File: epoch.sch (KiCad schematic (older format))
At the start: 32 parts, among them P1 USB_OTG, P2 BATT, P3 CONN_01X10, P4 CONN_02X05, Q1 Q_PMOS_DGS, SW1 SW_Push, U1 MIC5219-3.3BM5, U2 ATSAMD21Ennc-AU, U3 MCP73831T-2ACI/OT, U4 MCP7940N-I/SN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

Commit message: Link buttons and add PCB
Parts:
- removed 10K1: R, symbol R
- removed C10: 1uF, symbol C_Small
- removed D1: LED, symbol LED
- removed D2: ZLLS410, symbol D
- removed P2: BATT, symbol CONN_01X02
- removed Q1: Q_PMOS_DGS, symbol Q_PMOS_DGS
- removed R4: 47K, symbol R
- removed U3: MCP73831T-2ACI/OT, smd-semi:SOT-23-5, symbol MCP73831T-2ACI/OT
- removed U4: MCP7940N-I/SN, IPC7351-Nominal:SOIC127P600X175-8, symbol MCP7940N-I/SN
- removed Y2: 32.768kHz, symbol Crystal
- added SW2: SW_Up, Buttons_Switches_THT:SW_PUSH_SMALL, symbol SW_Push
- added SW3: SW_Middle, Buttons_Switches_THT:SW_PUSH_SMALL, symbol SW_Push
- added SW4: SW_Down, Buttons_Switches_THT:SW_PUSH_SMALL, symbol SW_Push
- added U3: DS3231MZ, Housings_SOIC:SOIC-8_3.9x4.9mm_Pitch1.27mm, symbol DS3231MZ
- C1, C11, C2, C3, C5, C6: footprint (none) -> Capacitors_SMD:C_0805_HandSoldering
- C4, C9: value 4.7uF -> 0.1uF; footprint (none) -> Capacitors_SMD:C_0805_HandSoldering
- C7, C8: value 22uF -> ??uF; footprint (none) -> Capacitors_SMD:C_0805_HandSoldering
- P1: footprint (none) -> Connectors_Molex:USB_Micro-B_Molex_47346-0001
- P3: footprint (none) -> Connector_FFC_FPC:MOLEX_0.5MM_505278
- P4: footprint (none) -> Pin_Headers:Pin_Header_Straight_2x05_Pitch1.27mm_SMD
- R1: value 220 -> 249; footprint (none) -> Resistors_SMD:R_0805_HandSoldering
- R2: value 5K6 -> 4.7K; footprint (none) -> Resistors_SMD:R_0805_HandSoldering
- R3: value 47K -> 4.7K; footprint (none) -> Resistors_SMD:R_0805_HandSoldering
- R5: footprint (none) -> Resistors_SMD:R_0805_HandSoldering
- SW1: value SW_Push -> SW_Reset; footprint (none) -> Buttons_Switches_THT:SW_PUSH_SMALL
- U2: footprint IPC7351-Nominal:QFP80P900X900X120-32 -> Housings_QFP:TQFP-32_7x7mm_Pitch0.8mm
- U5: footprint (none) -> TO_SOT_Packages_SMD:SOT-353_SC-70-5_Handsoldering
- Y1: footprint (none) -> Crystals:Crystals_Citizen_CM200C_7.9_x_3.7
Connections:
- net labels added: BUT_DWN, BUT_MID, BUT_UP
- net labels removed: (+5), PWR_SENSE, STAT, SWCLK
- wire segments 116 -> 93
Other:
- note added: "Real Time clock and VCOM refresh"
- note added: "USB"
- note removed: "USB Charging Circuit"
- moved on the sheet: C1, C2, C3, C5, C6, C7, C8, P1, R5, SW1, U1, U2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

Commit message: More Layout
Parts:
- removed P1: USB_OTG, Connectors_Molex:USB_Micro-B_Molex_47346-0001, symbol USB_OTG
- added J1: USB_OTG, Connectors:USB-MICROB_LARGEPAD, symbol USB_OTG
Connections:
- net (GND): now also J1.5 (GND), J1.6 (Shield)
- net USB_D+: now also J1.3 (D+)
- net USB_D-: now also J1.2 (D-)
- net at U1.1 (IN), U1.3 (EN): now also J1.1 (VBUS)
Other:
- note removed: "USB"
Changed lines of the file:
@@
 RESET
-$Comp
-L USB_OTG P1
-U 1 1 58B3A824
-P 1750 1350
-F 0 "P1" H 1900 950 50  0000 C CNN
-F 1 "USB_OTG" H 1750 1700 50  0000 C CNN
-F 2 "Connectors_Molex:USB_Micro-B_Molex_47346-0001" V 1700 1250 50  0001 C CNN
-F 3 "" V 1700 1250 50  0000 C CNN
-	1    1750 1350
-	1    0    0    1
-$EndComp
 $Comp
 L (GND) #PWR010
 U 1 1 58B3A991
-P 1450 1850
-F 0 "#PWR010" H 1450 1850 30  0001 C CNN
-F 1 "(GND)" H 1450 1850 30  0001 C CNN
-F 2 "" H 1450 1850 60  0000 C CNN
-F 3 "" H 1450 1850 60  0000 C CNN
-	1    1450 1850
+P 1600 2000
+F 0 "#PWR010" H 1600 2000 30  0001 C CNN
+F 1 "(GND)" H 1600 2000 30  0001 C CNN
+F 2 "" H 1600 2000 60  0000 C CNN
+F 3 "" H 1600 2000 60  0000 C CNN
+	1    1600 2000
 	-1   0    0    -1
 $EndComp
-Text GLabel 2050 1250 2    60   BiDi ~ 0
+Text GLabel 2000 1500 2    60   BiDi ~ 0
 USB_D-
-Text GLabel 2050 1350 2    60   BiDi ~ 0
+Text GLabel 2000 1400 2    60   BiDi ~ 0
 USB_D+
 $Comp
@@
 	1    0    0    -1
 $EndComp
-Wire Wire Line
-	2800 1250 3050 1250
 $Comp
 L (GND) #PWR011
@@
 Wire Wire Line
 	4350 1150 4350 1200
-Text Notes 1550 850  0    60   ~ 0
-USB
 Text Notes 3050 850  0    60   ~ 0
 3.3V Regulator
@@
 	8500 2150 8500 2600
 Wire Wire Line
-	1650 950  1650 900
-Wire Wire Line
-	1450 900  1750 900
-Wire Wire Line
-	1450 900  1450 1850
-Wire Wire Line
-	1750 900  1750 950
-Connection ~ 1650 900
-Wire Wire Line
-	2800 1550 2050 1550
-Wire Wire Line
-	2800 1150 2800 1550
+	2800 1150 2800 1250
 Wire Wire Line
 	2800 1150 3050 1150
-Connection ~ 2800 1250
+Connection ~ 2800 1200
 $Comp
 L SW_Push SW2
@@
 SDA
 Wire Wire Line
-	6600 1850 6400 1850
-Wire Wire Line
-	6600 1950 6000 1950
+	6400 1850 6600 1850
+Wire Wire Line
+	6000 1950 6600 1950
 $Comp
 L R R3
@@
 Connection ~ 6050 1950
 Wire Wire Line
-	6050 1500 6050 1350
+	6050 1350 6050 1500
 Wire Wire Line
 	6500 1850 6500 1800
@@
 Text GLabel 3750 4600 2    60   Input ~ 0
 BUT_UP
+$Comp
+L USB_OTG J1
+U 1 1 58F5A24A
+P 1700 1400
+F 0 "J1" H 1500 1850 50  0000 L CNN
+F 1 "USB_OTG" H 1500 1750 50  0000 L CNN
+F 2 "Connectors:USB-MICROB_LARGEPAD" H 1850 1350 50  0001 C CNN
+F 3 "" H 1850 1350 50  0001 C CNN
+	1    1700 1400
+	1    0    0    -1
+$EndComp
+Wire Wire Line
+	2800 1250 3050 1250
+Wire Wire Line
+	1600 1800 1600 2000
+Wire Wire Line
+	1700 1800 1700 1900
+Wire Wire Line
+	1700 1900 1600 1900
+Connection ~ 1600 1900
+Wire Wire Line
+	2000 1200 2800 1200
 $EndSCHEMATC

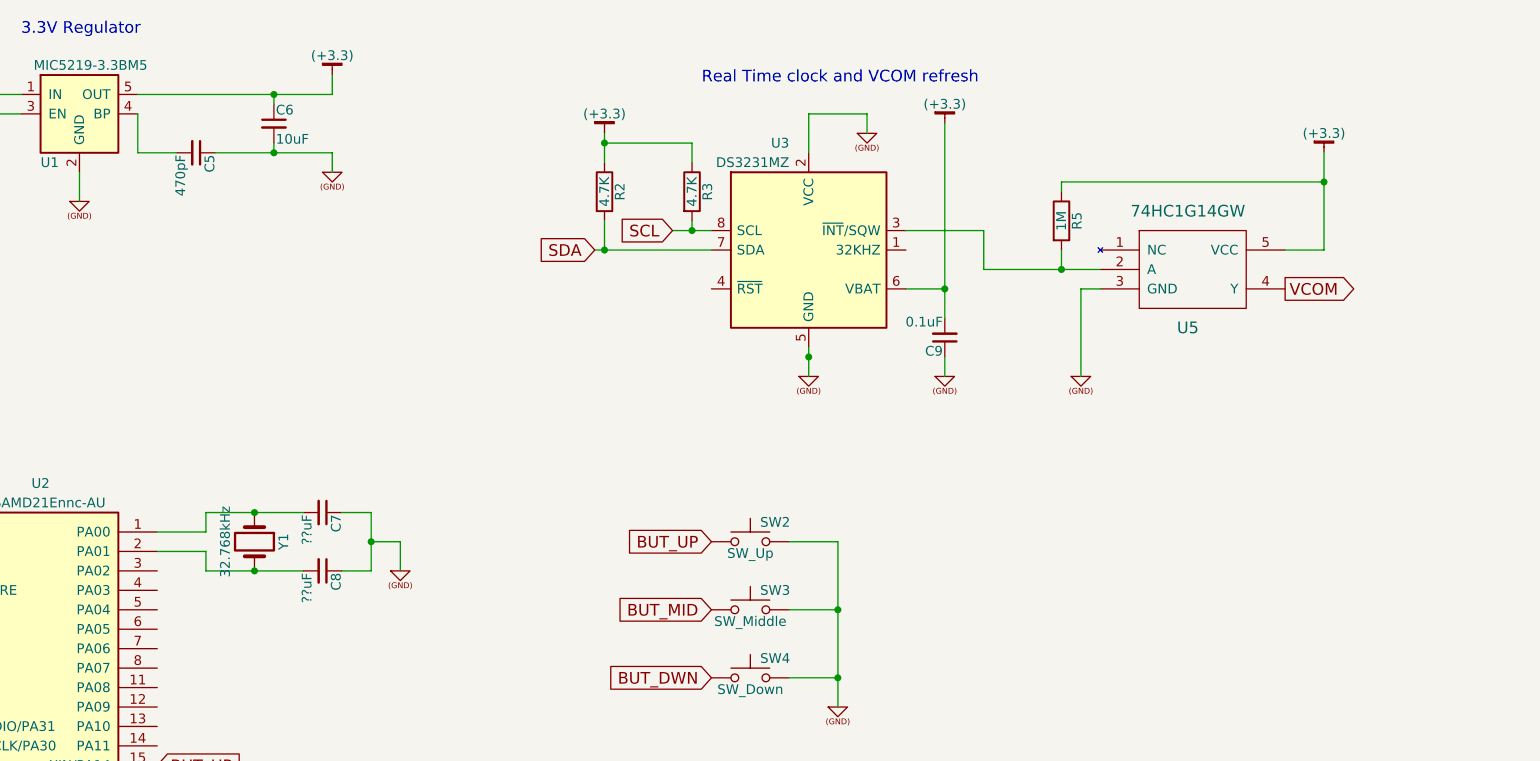
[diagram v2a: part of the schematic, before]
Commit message: Add coincell
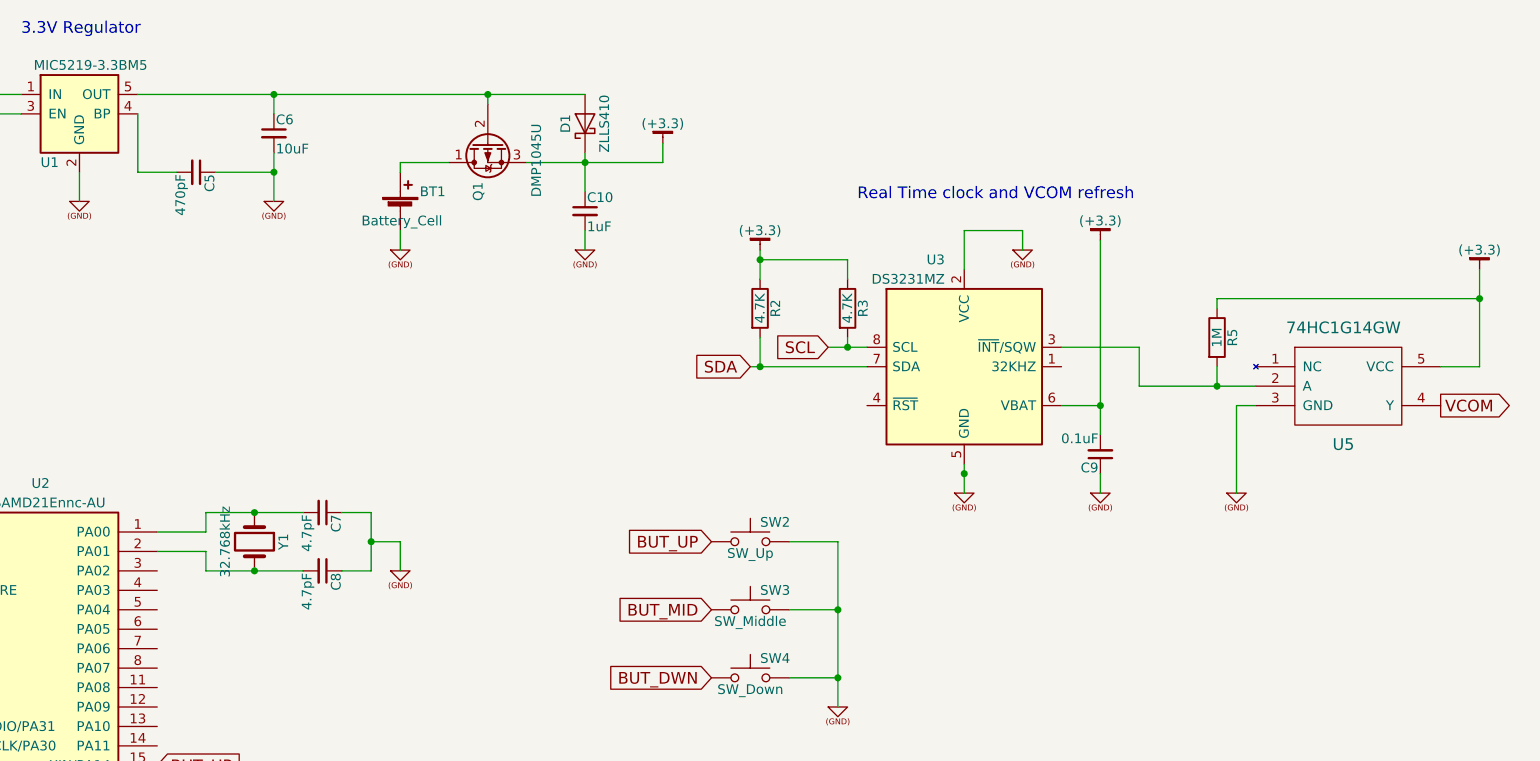
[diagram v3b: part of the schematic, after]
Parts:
- added BT1: Battery_Cell, my-fp-library:CR2032-001, symbol Battery_Cell
- added C10: 1uF, Capacitors_SMD:C_0805_HandSoldering, symbol C_Small
- added D1: ZLLS410, symbol D_Schottky
- added Q1: DMP1045U, symbol Q_PMOS_DGS
- C7, C8: value ??uF -> 4.7pF
- P3: footprint Connector_FFC_FPC:MOLEX_0.5MM_505278 -> my-fp-library:MOLEX_0.5MM_505278
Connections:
- net (+3.3): now also C10.1, D1.1 (K), Q1.3 (S); no longer C6.1, U1.5 (OUT)
- net (GND): now also BT1.2 (-), C10.2
- new net: C6.1, D1.2 (A), Q1.2 (G), U1.5 (OUT)
- new net: BT1.1 (+), Q1.1 (D)
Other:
- moved on the sheet: C5, C6, C9, R2, R3, R5, U3, U5

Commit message: Battery parts
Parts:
- D1: footprint (none) -> Diodes_SMD:D_SOD-323_HandSoldering
- Q1: footprint (none) -> TO_SOT_Packages_SMD:SOT-23_Handsoldering
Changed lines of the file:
@@
 F 0 "D1" H 5950 1400 50  0000 C CNN
 F 1 "ZLLS410" H 5950 1200 50  0000 C CNN
-F 2 "" H 5950 1300 50  0001 C CNN
+F 2 "Diodes_SMD:D_SOD-323_HandSoldering" H 5950 1300 50  0001 C CNN
 F 3 "" H 5950 1300 50  0001 C CNN
 	1    5950 1300
@@
 F 0 "Q1" H 5650 1450 50  0000 L CNN
 F 1 "DMP1045U" H 5350 1150 50  0000 L CNN
-F 2 "" H 5650 1500 50  0001 C CNN
+F 2 "TO_SOT_Packages_SMD:SOT-23_Handsoldering" H 5650 1500 50  0001 C CNN
 F 3 "" H 5450 1400 50  0001 C CNN
 	1    5450 1400

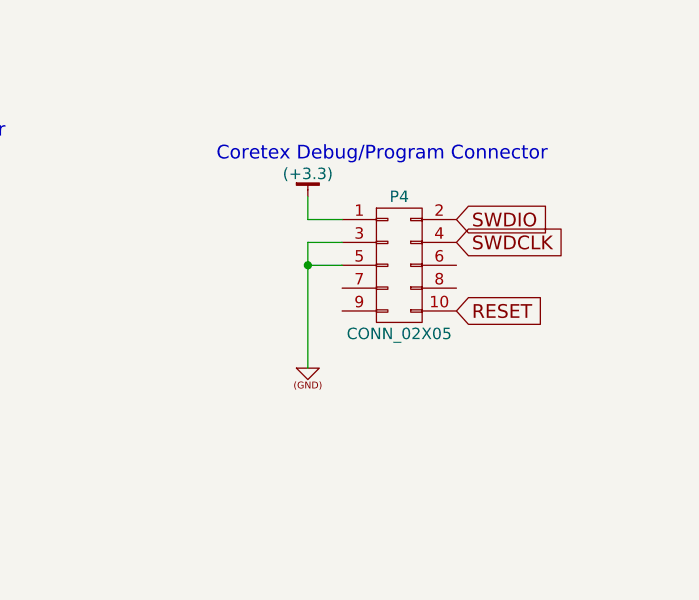
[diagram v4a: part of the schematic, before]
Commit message: More connections and change battery to pads
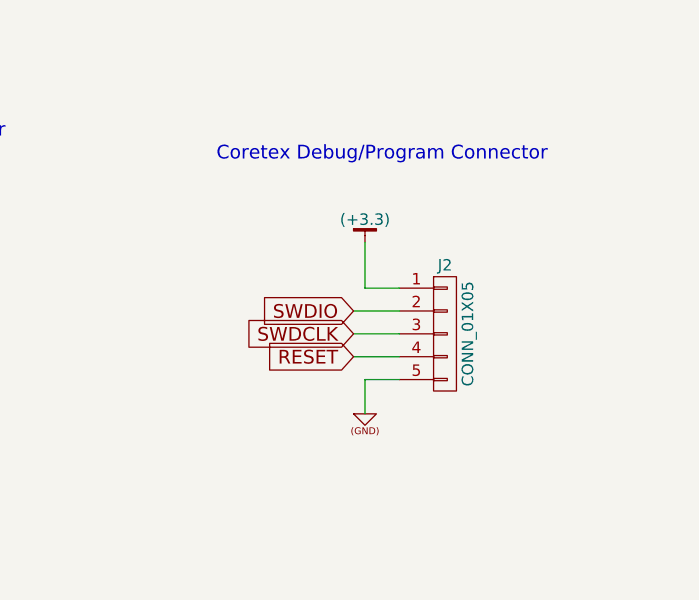
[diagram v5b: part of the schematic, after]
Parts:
- removed P4: CONN_02X05, Pin_Headers:Pin_Header_Straight_2x05_Pitch1.27mm_SMD, symbol CONN_02X05
- added J2: CONN_01X05, Pin_Headers:Pin_Header_Straight_1x05_Pitch1.27mm, symbol CONN_01X05
- BT1: footprint my-fp-library:CR2032-001 -> Pin_Headers:Pin_Header_Straight_2x01_Pitch2.54mm_SMD
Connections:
- net (+3.3): now also J2.1 (P1)
- net (GND): now also J2.5 (P5)
- net RESET: now also J2.4 (P4)
- net SWDCLK: now also J2.3 (P3)
- net SWDIO: now also J2.2 (P2)
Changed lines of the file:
@@
 Coretex Debug/Program Connector
 $Comp
-L CONN_02X05 P4
-U 1 1 58B3A30B
-P 9550 5400
-F 0 "P4" H 9550 5700 50  0000 C CNN
-F 1 "CONN_02X05" H 9550 5100 50  0000 C CNN
-F 2 "Pin_Headers:Pin_Header_Straight_2x05_Pitch1.27mm_SMD" H 9550 4200 50  0001 C CNN
-F 3 "" H 9550 4200 50  0000 C CNN
-	1    9550 5400
-	1    0    0    -1
-$EndComp
-Text GLabel 9800 5200 2    60   Input ~ 0
-SWDIO
-Text GLabel 9800 5300 2    60   Input ~ 0
-SWDCLK
-$Comp
-L (+3.3) #PWR08
-U 1 1 58B3A4FA
-P 9150 5100
-F 0 "#PWR08" H 9150 5150 30  0001 C CNN
-F 1 "(+3.3)" H 9150 5200 50  0000 C CNN
-F 2 "" H 9150 5100 60  0000 C CNN
-F 3 "" H 9150 5100 60  0000 C CNN
-	1    9150 5100
-	1    0    0    -1
-$EndComp
-Wire Wire Line
-	9300 5200 9150 5200
-Wire Wire Line
-	9150 5200 9150 5100
-$Comp
-L (GND) #PWR09
-U 1 1 58B3A5DF
-P 9150 5850
-F 0 "#PWR09" H 9150 5850 30  0001 C CNN
-F 1 "(GND)" H 9150 5850 30  0001 C CNN
-F 2 "" H 9150 5850 60  0000 C CNN
-F 3 "" H 9150 5850 60  0000 C CNN
-	1    9150 5850
-	1    0    0    -1
-$EndComp
-Wire Wire Line
-	9300 5300 9150 5300
-Wire Wire Line
-	9150 5300 9150 5850
-Wire Wire Line
-	9300 5400 9150 5400
-Connection ~ 9150 5400
-Text GLabel 9800 5600 2    60   Input ~ 0
-RESET
-$Comp
-L (GND) #PWR010
+L (GND) #PWR08
 U 1 1 58B3A991
 P 1600 2000
-F 0 "#PWR010" H 1600 2000 30  0001 C CNN
+F 0 "#PWR08" H 1600 2000 30  0001 C CNN
 F 1 "(GND)" H 1600 2000 30  0001 C CNN
 F 2 "" H 1600 2000 60  0000 C CNN
@@
 $EndComp
 $Comp
-L (GND) #PWR011
+L (GND) #PWR09
 U 1 1 58B44D3A
 P 3350 1700
-F 0 "#PWR011" H 3350 1700 30  0001 C CNN
+F 0 "#PWR09" H 3350 1700 30  0001 C CNN
 F 1 "(GND)" H 3350 1700 30  0001 C CNN
 F 2 "" H 3350 1700 60  0000 C CNN
@@
 $EndComp
 $Comp
-L (GND) #PWR012
+L (GND) #PWR010
 U 1 1 58B45265
 P 4350 1700
-F 0 "#PWR012" H 4350 1700 30  0001 C CNN
+F 0 "#PWR010" H 4350 1700 30  0001 C CNN
 F 1 "(GND)" H 4350 1700 30  0001 C CNN
 F 2 "" H 4350 1700 60  0000 C CNN
@@
 RESET
 $Comp
-L (GND) #PWR013
+L (GND) #PWR011
 U 1 1 58B4CFC2
 P 3800 6750
-F 0 "#PWR013" H 3800 6750 30  0001 C CNN
+F 0 "#PWR011" H 3800 6750 30  0001 C CNN
 F 1 "(GND)" H 3800 6750 30  0001 C CNN
 F 2 "" H 3800 6750 60  0000 C CNN
@@
 EXTMODE
 $Comp
-L (GND) #PWR014
+L (GND) #PWR012
 U 1 1 58B4E10C
 P 6800 6100
-F 0 "#PWR014" H 6800 6100 30  0001 C CNN
+F 0 "#PWR012" H 6800 6100 30  0001 C CNN
 F 1 "(GND)" H 6800 6100 30  0001 C CNN
 F 2 "" H 6800 6100 60  0000 C CNN
@@
 Connection ~ 6800 5600
 $Comp
-L (+3.3) #PWR015
+L (+3.3) #PWR013
 U 1 1 58B4E512
 P 6400 5300
-F 0 "#PWR015" H 6400 5350 30  0001 C CNN
+F 0 "#PWR013" H 6400 5350 30  0001 C CNN
 F 1 "(+3.3)" H 6400 5400 50  0000 C CNN
 F 2 "" H 6400 5300 60  0000 C CNN
@@
 $EndComp
 $Comp
-L (GND) #PWR016
+L (GND) #PWR014
 U 1 1 58B4E562
 P 6400 6100
-F 0 "#PWR016" H 6400 6100 30  0001 C CNN
+F 0 "#PWR014" H 6400 6100 30  0001 C CNN
 F 1 "(GND)" H 6400 6100 30  0001 C CNN
 F 2 "" H 6400 6100 60  0000 C CNN
@@
 	8800 2650 9400 2650
 $Comp
-L (+3.3) #PWR017
+L (+3.3) #PWR015
 U 1 1 58BA5A7F
 P 10550 2050
-F 0 "#PWR017" H 10550 2100 30  0001 C CNN
+F 0 "#PWR015" H 10550 2100 30  0001 C CNN
 F 1 "(+3.3)" H 10550 2150 50  0000 C CNN
 F 2 "" H 10550 2050 60  0000 C CNN
@@
 	2650 6550 2800 6550
 $Comp
-L (GND) #PWR018
+L (GND) #PWR016
 U 1 1 58E707F3
 P 2750 7000
-F 0 "#PWR018" H 2750 7000 30  0001 C CNN
+F 0 "#PWR016" H 2750 7000 30  0001 C CNN
 F 1 "(GND)" H 2750 7000 30  0001 C CNN
 F 2 "" H 2750 7000 60  0000 C CNN
@@
 $EndComp
 $Comp
-L (GND) #PWR019
+L (GND) #PWR017
 U 1 1 58E6E62D
 P 7900 3200
-F 0 "#PWR019" H 7900 3200 30  0001 C CNN
+F 0 "#PWR017" H 7900 3200 30  0001 C CNN
 F 1 "(GND)" H 7900 3200 30  0001 C CNN
 F 2 "" H 7900 3200 60  0000 C CNN
@@
 Connection ~ 7900 3100
 $Comp
-L (+3.3) #PWR020
+L (+3.3) #PWR018
 U 1 1 58E6F996
 P 8600 1900
-F 0 "#PWR020" H 8600 1950 30  0001 C CNN
+F 0 "#PWR018" H 8600 1950 30  0001 C CNN
 F 1 "(+3.3)" H 8600 2000 50  0000 C CNN
 F 2 "" H 8600 1900 60  0000 C CNN
@@
 $EndComp
 $Comp
-L (GND) #PWR021
+L (GND) #PWR019
 U 1 1 58E70274
 P 8600 3200
-F 0 "#PWR021" H 8600 3200 30  0001 C CNN
+F 0 "#PWR019" H 8600 3200 30  0001 C CNN
 F 1 "(GND)" H 8600 3200 30  0001 C CNN
 F 2 "" H 8600 3200 60  0000 C CNN
@@
 Connection ~ 8600 2750
 $Comp
-L (GND) #PWR022
+L (GND) #PWR020
 U 1 1 58E721AF
 P 9300 3200
-F 0 "#PWR022" H 9300 3200 30  0001 C CNN
+F 0 "#PWR020" H 9300 3200 30  0001 C CNN
 F 1 "(GND)" H 9300 3200 30  0001 C CNN
 F 2 "" H 9300 3200 60  0000 C CNN
@@
 $EndComp
 $Comp
-L (+3.3) #PWR023
+L (+3.3) #PWR021
 U 1 1 58E7CBC3
 P 6850 1950
-F 0 "#PWR023" H 6850 2000 30  0001 C CNN
+F 0 "#PWR021" H 6850 2000 30  0001 C CNN
 F 1 "(+3.3)" H 6850 2050 50  0000 C CNN
 F 2 "" H 6850 1950 60  0000 C CNN
@@
 Connection ~ 6850 2000
 $Comp
-L (GND) #PWR024
+L (GND) #PWR022
 U 1 1 58E7CF05
 P 8200 1950
-F 0 "#PWR024" H 8200 1950 30  0001 C CNN
+F 0 "#PWR022" H 8200 1950 30  0001 C CNN
 F 1 "(GND)" H 8200 1950 30  0001 C CNN
 F 2 "" H 8200 1950 60  0000 C CNN
@@
 	8200 1850 8200 1950
 $Comp
-L (GND) #PWR025
+L (GND) #PWR023
 U 1 1 58E7E41A
 P 7250 4300
-F 0 "#PWR025" H 7250 4300 30  0001 C CNN
+F 0 "#PWR023" H 7250 4300 30  0001 C CNN
 F 1 "(GND)" H 7250 4300 30  0001 C CNN
 F 2 "" H 7250 4300 60  0000 C CNN
@@
 F 0 "BT1" H 5100 1850 50  0000 L CNN
 F 1 "Battery_Cell" H 4800 1700 50  0000 L CNN
-F 2 "my-fp-library:CR2032-001" V 5000 1810 50  0001 C CNN
+F 2 "Pin_Headers:Pin_Header_Straight_2x01_Pitch2.54mm_SMD" V 5000 1810 50  0001 C CNN
 F 3 "" V 5000 1810 50  0001 C CNN
 	1    5000 1750
@@
 $EndComp
 $Comp
-L (+3.3) #PWR026
+L (+3.3) #PWR024
 U 1 1 58F973F0
 P 6350 1400
-F 0 "#PWR026" H 6350 1450 30  0001 C CNN
+F 0 "#PWR024" H 6350 1450 30  0001 C CNN
 F 1 "(+3.3)" H 6350 1500 50  0000 C CNN
 F 2 "" H 6350 1400 60  0000 C CNN
@@
 $EndComp
 $Comp
-L (GND) #PWR027
+L (GND) #PWR025
 U 1 1 58F9887B
 P 5950 1950
-F 0 "#PWR027" H 5950 1950 30  0001 C CNN
+F 0 "#PWR025" H 5950 1950 30  0001 C CNN
 F 1 "(GND)" H 5950 1950 30  0001 C CNN
 F 2 "" H 5950 1950 60  0000 C CNN
@@
 Connection ~ 5450 1150
 $Comp
-L (GND) #PWR028
+L (GND) #PWR026
 U 1 1 58F99ADF
 P 5000 1950
-F 0 "#PWR028" H 5000 1950 30  0001 C CNN
+F 0 "#PWR026" H 5000 1950 30  0001 C CNN
 F 1 "(GND)" H 5000 1950 30  0001 C CNN
 F 2 "" H 5000 1950 60  0000 C CNN
@@
 Wire Wire Line
 	5000 1950 5000 1850
+$Comp
+L CONN_01X05 J2
+U 1 1 58FD226D
+P 9750 5700
+F 0 "J2" H 9750 6000 50  0000 C CNN
+F 1 "CONN_01X05" V 9850 5700 50  0000 C CNN
+F 2 "Pin_Headers:Pin_Header_Straight_1x05_Pitch1.27mm" H 9750 5700 50  0001 C CNN
+F 3 "" H 9750 5700 50  0001 C CNN
+	1    9750 5700
+	1    0    0    -1
+$EndComp
+$Comp
+L (+3.3) #PWR027
+U 1 1 58FD27AF
+P 9400 5300
+F 0 "#PWR027" H 9400 5350 30  0001 C CNN
+F 1 "(+3.3)" H 9400 5400 50  0000 C CNN
+F 2 "" H 9400 5300 60  0000 C CNN
+F 3 "" H 9400 5300 60  0000 C CNN
+	1    9400 5300
+	1    0    0    -1
+$EndComp
+Text GLabel 9350 5600 0    60   Input ~ 0
+SWDIO
+Text GLabel 9350 5700 0    60   Input ~ 0
+SWDCLK
+Text GLabel 9350 5800 0    60   Input ~ 0
+RESET
+$Comp
+L (GND) #PWR028
+U 1 1 58FD2934
+P 9400 6050
+F 0 "#PWR028" H 9400 6050 30  0001 C CNN
+F 1 "(GND)" H 9400 6050 30  0001 C CNN
+F 2 "" H 9400 6050 60  0000 C CNN
+F 3 "" H 9400 6050 60  0000 C CNN
+	1    9400 6050
+	1    0    0    -1
+$EndComp
+Wire Wire Line
+	9550 5600 9350 5600
+Wire Wire Line
+	9550 5700 9350 5700
+Wire Wire Line
+	9550 5800 9350 5800
+Wire Wire Line
+	9550 5900 9400 5900
+Wire Wire Line
+	9400 5900 9400 6050
+Wire Wire Line
+	9550 5500 9400 5500
+Wire Wire Line
+	9400 5500 9400 5300
 $EndSCHEMATC

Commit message: Complete connections
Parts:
- SW1, SW2, SW3, SW4: footprint Buttons_Switches_THT:SW_PUSH_SMALL -> Buttons_Switches_SMD:SW_SPST_B3U-1100P
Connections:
- net BUT_DWN: now also U2.21 (PA22); no longer U2.16 (XOUT/PA15)
- net BUT_MID: now also U2.16 (XOUT/PA15); no longer U2.21 (PA22)
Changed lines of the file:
@@
 F 0 "SW1" H 3550 6650 50  0000 L CNN
 F 1 "SW_Reset" H 3500 6490 50  0000 C CNN
-F 2 "Buttons_Switches_THT:SW_PUSH_SMALL" H 3500 6750 50  0001 C CNN
+F 2 "Buttons_Switches_SMD:SW_SPST_B3U-1100P" H 3500 6750 50  0001 C CNN
 F 3 "" H 3500 6750 50  0000 C CNN
 	1    3500 6550
@@
 F 0 "SW2" H 6850 3550 50  0000 L CNN
 F 1 "SW_Up" H 6800 3390 50  0000 C CNN
-F 2 "Buttons_Switches_THT:SW_PUSH_SMALL" H 6800 3650 50  0001 C CNN
+F 2 "Buttons_Switches_SMD:SW_SPST_B3U-1100P" H 6800 3650 50  0001 C CNN
 F 3 "" H 6800 3650 50  0001 C CNN
 	1    6800 3450
@@
 F 0 "SW3" H 6850 3900 50  0000 L CNN
 F 1 "SW_Middle" H 6800 3740 50  0000 C CNN
-F 2 "Buttons_Switches_THT:SW_PUSH_SMALL" H 6800 4000 50  0001 C CNN
+F 2 "Buttons_Switches_SMD:SW_SPST_B3U-1100P" H 6800 4000 50  0001 C CNN
 F 3 "" H 6800 4000 50  0001 C CNN
 	1    6800 3800
@@
 F 0 "SW4" H 6850 4250 50  0000 L CNN
 F 1 "SW_Down" H 6800 4090 50  0000 C CNN
-F 2 "Buttons_Switches_THT:SW_PUSH_SMALL" H 6800 4350 50  0001 C CNN
+F 2 "Buttons_Switches_SMD:SW_SPST_B3U-1100P" H 6800 4350 50  0001 C CNN
 F 3 "" H 6800 4350 50  0001 C CNN
 	1    6800 4150
@@
 Text GLabel 6600 4150 0    60   Input ~ 0
 BUT_DWN
+Text GLabel 3750 4700 2    60   Input ~ 0
+BUT_MID
 Text GLabel 3750 5200 2    60   Input ~ 0
-BUT_MID
-Text GLabel 3750 4700 2    60   Input ~ 0
 BUT_DWN
 Text GLabel 3750 4600 2    60   Input ~ 0
